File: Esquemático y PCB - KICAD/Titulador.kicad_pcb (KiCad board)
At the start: 2 copper layers, 160 x 95 mm, 32 parts, among them J1 1x2_F, J2 1x6_F, J3 1x4_F, J4 1x2_F, J5 1x5_F, J6 1x2_F, J7 1x4_F, Q1 BC548, SW1 SW_DIP_x04, U1 ESP32-DEVKITC-32D

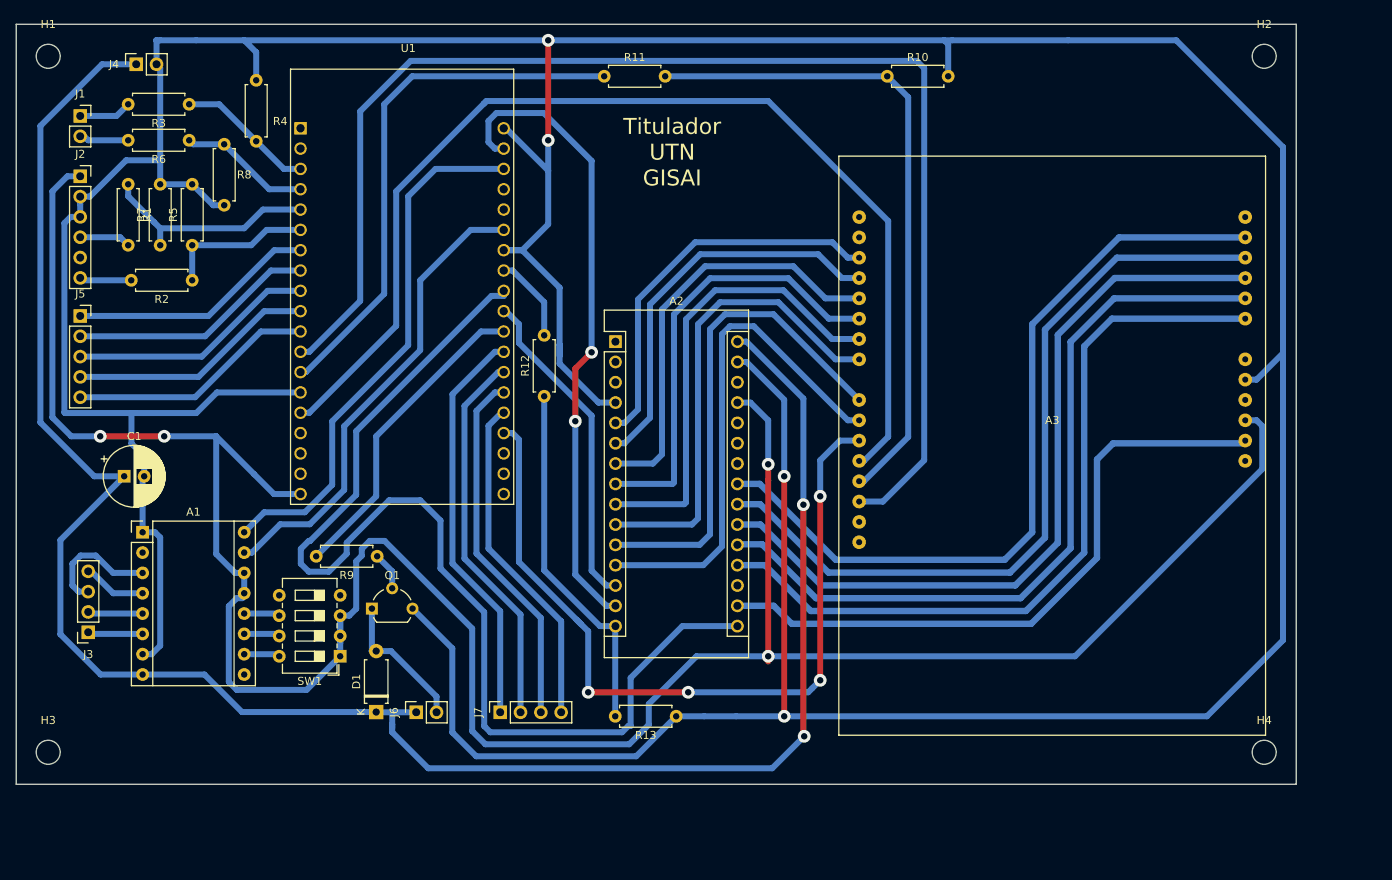
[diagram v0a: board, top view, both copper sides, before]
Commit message: Se finaliza pcb y corrige segun primera revision
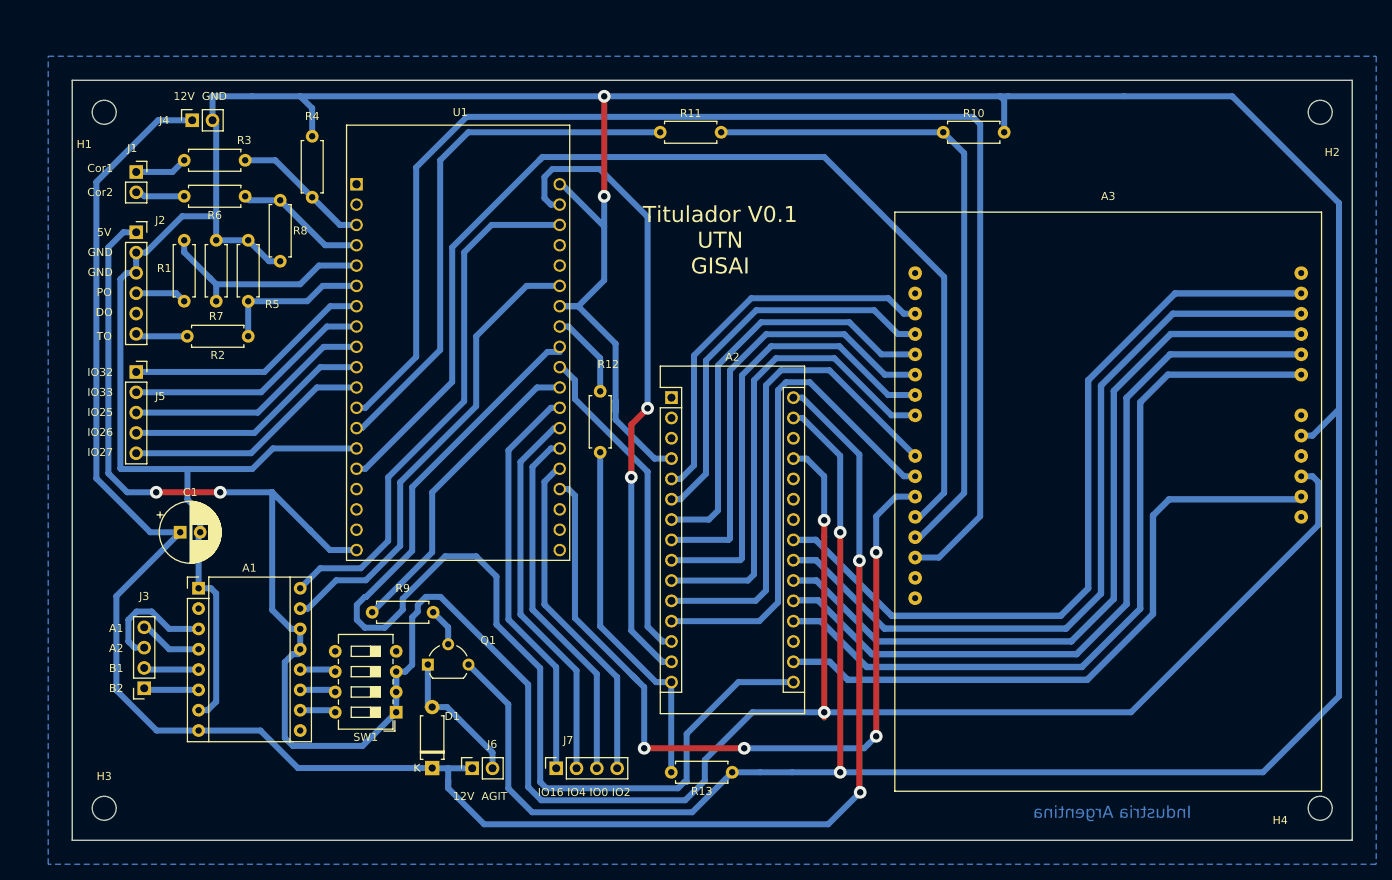
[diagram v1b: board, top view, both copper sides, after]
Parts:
- moved R4 9.90 mm to (109.0, 64.6)
- moved A1 9.90 mm to (94.8, 113.5)
- moved A2 9.90 mm to (153.9, 89.7)
- moved A3 9.90 mm to (208.5, 99.5)
- moved C1 9.90 mm to (92.5, 106.5)
- moved D1 9.90 mm to (124.0, 136.0)
- moved H1 9.90 mm to (83.0, 54.0)
- moved H2 9.90 mm to (235.0, 54.0)
- moved H3 9.90 mm to (83.0, 141.0)
- moved H4 9.90 mm to (235.0, 141.0)
- moved J1 9.90 mm to (87.0, 61.5)
- moved J2 9.90 mm to (87.0, 69.0)
- moved J3 9.90 mm to (88.0, 126.0)
- moved J4 9.90 mm to (94.0, 55.0)
- moved J5 9.90 mm to (87.0, 86.5)
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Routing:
- added copper zone on B.Cu, net GND
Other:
- board text added: "* Se toman las capacidades de fabricacion nacional, tomando como referencia Mayer SA. *Valores de grilla: Para orden de componentes: 1 mm. Para routeo: 0,5 mm. *Margen general 0,75 mm *Ancho de pista: 0,75 mm *Vías: 1,6 mm / 0,8 mm *Terminaciones: Cu + Flux"
- board text added: "12V AGIT"
- board text added: "12V GND"
- board text added: "5V"
- board text added: "A1"
- board text added: "A2"
- board text added: "B1"
- board text added: "B2"
- board text added: "Cor1"
- board text added: "Cor2"
- board text added: "DO"
- board text added: "GND"
- board text added: "IO16 IO4 IO0 IO2"
- board text added: "IO25"
- board text added: "IO26"
- board text added: "IO27"
- board text added: "IO32"
- board text added: "IO33"
- board text added: "Industria Argentina"
- board text added: "PO"
- board text added: "TO"
- board text added: "Titulador V0.1 UTN GISAI"
- board text removed: "Titulador UTN GISAI"

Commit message: Correcciones revision pcb
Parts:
- moved Q1 8.60 mm to (128.5, 130.0)
- moved R9 7.36 mm to (128.4, 122.5), turned to 90 degrees
- moved R4 0.63 mm to (109.5, 65.0)
- turned R8 to 90 degrees
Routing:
- net /VCLK: track 138.0 -> 108.6 mm
- net +5V: track 325.8 -> 316.9 mm
- net /Agitador: track 39.5 -> 32.9 mm
- net Net-(D1-Pad2): track 17.7 -> 12.4 mm
- net GND: track 600.6 -> 597.1 mm
- net Net-(Q1-Pad2): track 4.78 -> 6.09 mm
- net /VMOSI: track 79.9 -> 78.9 mm
